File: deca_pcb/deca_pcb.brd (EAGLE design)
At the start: 68.2 x 80 mm, 3 parts, among them IC1 DWM1000, U1 ATMEGA328P-PU

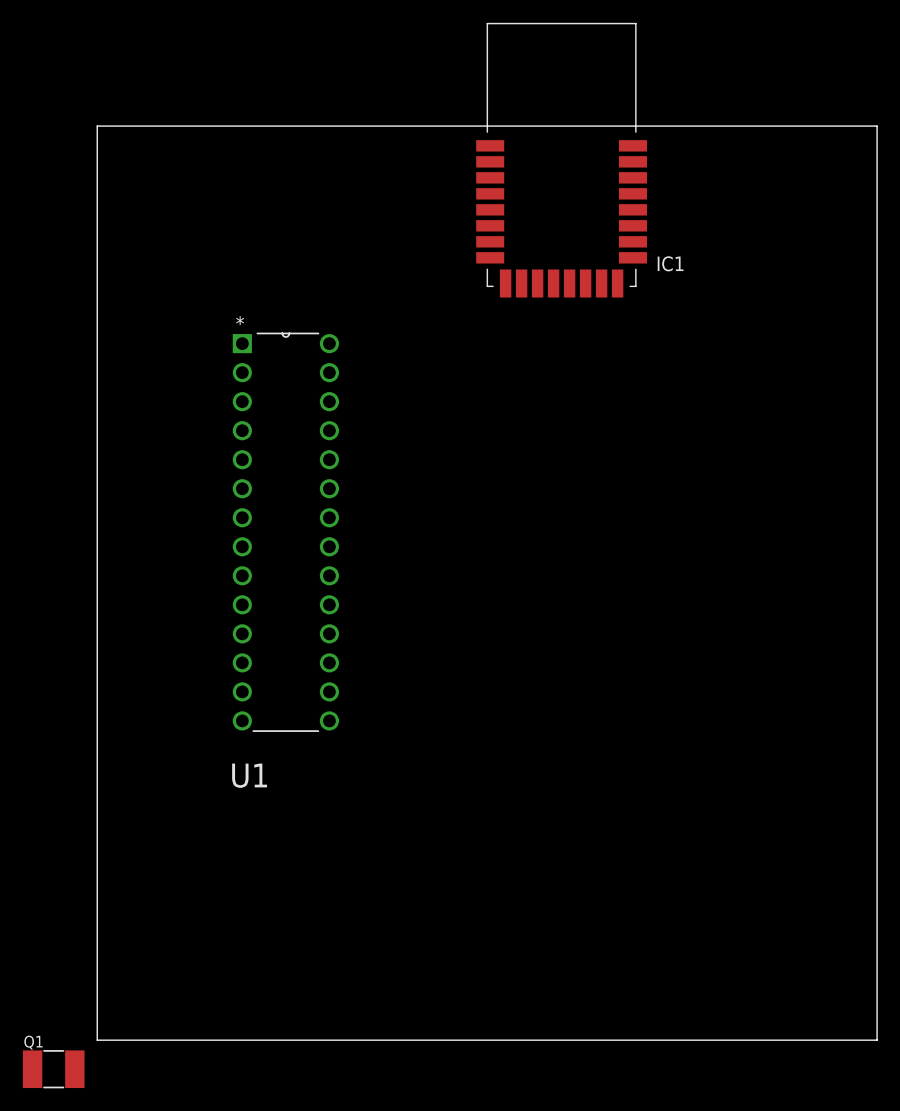
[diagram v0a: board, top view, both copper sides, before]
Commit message: added components
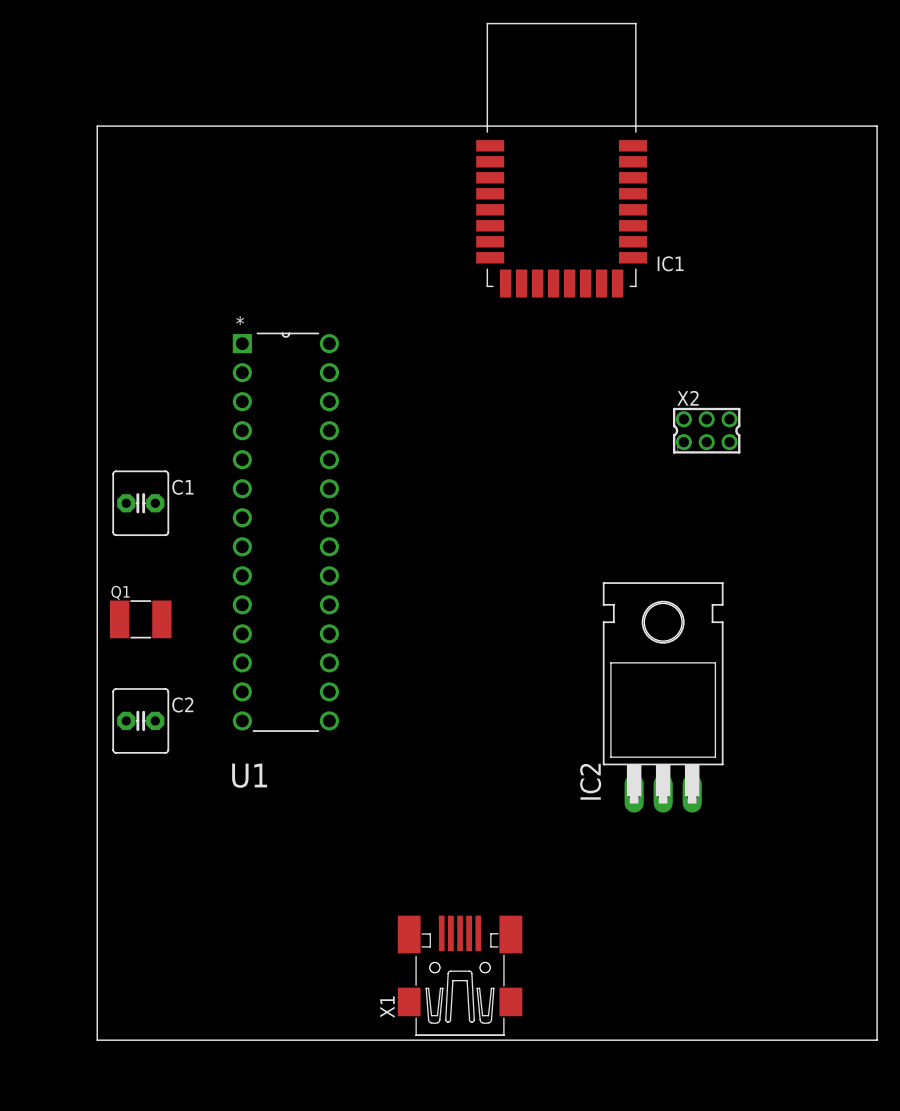
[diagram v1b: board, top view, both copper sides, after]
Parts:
- added C1, C2: (no value), capacitor-wima:C2.5-6
- added IC2: LM340H-18, linear:TO220H
- added X1: MINI-USB-32005-301, con-cypressindustries:32005-301
- added X2: 332-06, con-garry:332-06
- moved Q1 40.1 mm to (3.81, 36.8)
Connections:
- removed net AVCC: U1.20
- removed net VCC: U1.7
- new net N$10: IC2.1, X1.1
- new net N$11: C1.2, C2.1, IC1.16, IC1.21, IC1.23, IC1.24, IC1.8, IC2.2, U1.22, U1.8, X1.5, X2.6
- new net N$12: IC1.5, IC1.6, IC1.7, IC2.3, U1.20, U1.7, X2.2
- new net N$9: U1.1, X2.5
- net N$1: now also X2.3
- net N$2: now also X2.1
- net N$3: now also X2.4
- net N$7: now also C2.2
- net N$8: now also C1.1
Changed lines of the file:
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@@
 <attribute name="VALUE" x="13.0556" y="64.135" size="2.0828" layer="27" ratio="10" rot="SR0"/>
 </element>
-<element name="Q1" library="crystal-geyer_V1_0" library_urn="urn:adsk.eagle:library:203" package="5.0X3.2_2" package3d_urn="urn:adsk.eagle:package:11930/1" value="" x="-3.81" y="-2.54" smashed="yes">
-<attribute name="NAME" x="-6.45" y="-0.64" size="1.016" layer="25"/>
-<attribute name="VALUE" x="-6.45" y="-5.44" size="1.016" layer="27"/>
+<element name="Q1" library="crystal-geyer_V1_0" library_urn="urn:adsk.eagle:library:203" package="5.0X3.2_2" package3d_urn="urn:adsk.eagle:package:11930/1" value="" x="3.81" y="36.83" smashed="yes">
+<attribute name="NAME" x="1.17" y="38.73" size="1.016" layer="25"/>
+<attribute name="VALUE" x="1.17" y="33.93" size="1.016" layer="27"/>
+</element>
+<element name="C1" library="capacitor-wima" library_urn="urn:adsk.eagle:library:116" package="C2.5-6" package3d_urn="urn:adsk.eagle:package:5406/1" value="" x="3.81" y="46.99" smashed="yes">
+<attribute name="NAME" x="6.477" y="47.752" size="1.27" layer="25" ratio="10"/>
+<attribute name="VALUE" x="1.905" y="44.577" size="1.27" layer="27" ratio="10"/>
+</element>
+<element name="C2" library="capacitor-wima" library_urn="urn:adsk.eagle:library:116" package="C2.5-6" package3d_urn="urn:adsk.eagle:package:5406/1" value="" x="3.81" y="27.94" smashed="yes">
+<attribute name="NAME" x="6.477" y="28.702" size="1.27" layer="25" ratio="10"/>
+<attribute name="VALUE" x="1.905" y="25.527" size="1.27" layer="27" ratio="10"/>
+</element>
+<element name="X1" library="con-cypressindustries" library_urn="urn:adsk.eagle:library:138" package="32005-301" package3d_urn="urn:adsk.eagle:package:6446/1" value="MINI-USB-32005-301" x="31.75" y="6.35" smashed="yes" rot="R90">
+<attribute name="MF" value="" x="31.75" y="6.35" size="1.778" layer="27" rot="R90" display="off"/>
+<attribute name="MPN" value="" x="31.75" y="6.35" size="1.778" layer="27" rot="R90" display="off"/>
+<attribute name="NAME" x="26.035" y="1.905" size="1.27" layer="25" rot="R90"/>
+<attribute name="OC_FARNELL" value="unknown" x="31.75" y="6.35" size="1.778" layer="27" rot="R90" display="off"/>
+<attribute name="OC_NEWARK" value="unknown" x="31.75" y="6.35" size="1.778" layer="27" rot="R90" display="off"/>
+<attribute name="VALUE" x="38.735" y="1.905" size="1.27" layer="27" rot="R90"/>
+</element>
+<element name="IC2" library="linear" library_urn="urn:adsk.eagle:library:262" package="TO220H" package3d_urn="urn:adsk.eagle:package:16414/1" value="LM340H-18" x="49.53" y="31.75" smashed="yes">
+<attribute name="NAME" x="44.069" y="20.828" size="1.778" layer="25" ratio="10" rot="R90"/>
+<attribute name="VALUE" x="56.896" y="20.701" size="1.778" layer="27" ratio="10" rot="R90"/>
+</element>
+<element name="X2" library="con-garry" library_urn="urn:adsk.eagle:library:147" package="332-06" package3d_urn="urn:adsk.eagle:package:6811/1" value="332-06" x="53.34" y="53.34" smashed="yes">
+<attribute name="NAME" x="50.72" y="55.53" size="1.27" layer="25"/>
+<attribute name="VALUE" x="50.72" y="56.88" size="1.27" layer="27"/>
 </element>
 </elements>
 <signals>
-<signal name="VCC">
-<contactref element="U1" pad="7"/>
-</signal>
-<signal name="AVCC">
-<contactref element="U1" pad="20"/>
-</signal>
 <signal name="N$1">
 <contactref element="U1" pad="19"/>
 <contactref element="IC1" pad="20"/>
+<contactref element="X2" pad="3"/>
 <wire x1="20.32" y1="38.1" x2="46.89" y2="72.67" width="0" layer="19" extent="1-1"/>
+<wire x1="53.34" y1="52.34" x2="20.32" y2="38.1" width="0" layer="19" extent="1-1"/>
 </signal>
 <signal name="N$2">
 <contactref element="U1" pad="18"/>
 <contactref element="IC1" pad="19"/>
+<contactref element="X2" pad="1"/>
 <wire x1="20.32" y1="35.56" x2="46.89" y2="71.27" width="0" layer="19" extent="1-1"/>
+<wire x1="51.34" y1="52.34" x2="20.32" y2="35.56" width="0" layer="19" extent="1-1"/>
 </signal>
 <signal name="N$3">
 <contactref element="U1" pad="17"/>
 <contactref element="IC1" pad="18"/>
+<contactref element="X2" pad="4"/>
 <wire x1="20.32" y1="33.02" x2="46.89" y2="69.87" width="0" layer="19" extent="1-1"/>
+<wire x1="53.34" y1="54.34" x2="20.32" y2="33.02" width="0" layer="19" extent="1-1"/>
 </signal>
 <signal name="N$4">
@@
 <contactref element="U1" pad="9"/>
 <contactref element="Q1" pad="2"/>
-<wire x1="-1.96" y1="-2.54" x2="12.7" y2="40.64" width="0" layer="19" extent="1-1"/>
+<contactref element="C2" pad="2"/>
+<wire x1="5.66" y1="36.83" x2="12.7" y2="40.64" width="0" layer="19" extent="1-1"/>
+<wire x1="5.08" y1="27.94" x2="5.66" y2="36.83" width="0" layer="19" extent="1-1"/>
 </signal>
 <signal name="N$8">
 <contactref element="U1" pad="10"/>
 <contactref element="Q1" pad="1"/>
-<wire x1="-5.66" y1="-2.54" x2="12.7" y2="38.1" width="0" layer="19" extent="1-1"/>
+<contactref element="C1" pad="1"/>
+<wire x1="1.96" y1="36.83" x2="12.7" y2="38.1" width="0" layer="19" extent="1-1"/>
+<wire x1="2.54" y1="46.99" x2="1.96" y2="36.83" width="0" layer="19" extent="1-1"/>
+</signal>
+<signal name="N$10">
+<contactref element="X1" pad="1"/>
+<contactref element="IC2" pad="1"/>
+<wire x1="30.15" y1="9.35" x2="46.99" y2="21.59" width="0" layer="19" extent="1-1"/>
+</signal>
+<signal name="N$11">
+<contactref element="X1" pad="5"/>
+<contactref element="IC2" pad="2"/>
+<contactref element="C1" pad="2"/>
+<contactref element="C2" pad="1"/>
+<contactref element="U1" pad="22"/>
+<contactref element="U1" pad="8"/>
+<contactref element="IC1" pad="21"/>
+<contactref element="IC1" pad="16"/>
+<contactref element="IC1" pad="23"/>
+<contactref element="IC1" pad="24"/>
+<contactref element="IC1" pad="8"/>
+<contactref element="X2" pad="6"/>
+<wire x1="46.89" y1="78.27" x2="46.89" y2="76.87" width="0" layer="19" extent="1-1"/>
+<wire x1="46.89" y1="74.07" x2="46.89" y2="76.87" width="0" layer="19" extent="1-1"/>
+<wire x1="45.54" y1="66.22" x2="46.89" y2="74.07" width="0" layer="19" extent="1-1"/>
+<wire x1="34.39" y1="68.47" x2="45.54" y2="66.22" width="0" layer="19" extent="1-1"/>
+<wire x1="20.32" y1="45.72" x2="34.39" y2="68.47" width="0" layer="19" extent="1-1"/>
+<wire x1="12.7" y1="43.18" x2="20.32" y2="45.72" width="0" layer="19" extent="1-1"/>
+<wire x1="5.08" y1="46.99" x2="12.7" y2="43.18" width="0" layer="19" extent="1-1"/>
+<wire x1="2.54" y1="27.94" x2="12.7" y2="43.18" width="0" layer="19" extent="1-1"/>
+<wire x1="55.34" y1="54.34" x2="2.54" y2="27.94" width="0" layer="19" extent="1-1"/>
+<wire x1="33.35" y1="9.35" x2="2.54" y2="27.94" width="0" layer="19" extent="1-1"/>
+<wire x1="49.53" y1="21.59" x2="33.35" y2="9.35" width="0" layer="19" extent="1-1"/>
+</signal>
+<signal name="N$12">
+<contactref element="IC2" pad="3"/>
+<contactref element="U1" pad="7"/>
+<contactref element="U1" pad="20"/>
+<contactref element="IC1" pad="5"/>
+<contactref element="IC1" pad="6"/>
+<contactref element="IC1" pad="7"/>
+<contactref element="X2" pad="2"/>
+<wire x1="34.39" y1="71.27" x2="34.39" y2="72.67" width="0" layer="19" extent="1-1"/>
+<wire x1="34.39" y1="69.87" x2="34.39" y2="71.27" width="0" layer="19" extent="1-1"/>
+<wire x1="20.32" y1="40.64" x2="34.39" y2="69.87" width="0" layer="19" extent="1-1"/>
+<wire x1="12.7" y1="45.72" x2="20.32" y2="40.64" width="0" layer="19" extent="1-1"/>
+<wire x1="52.07" y1="21.59" x2="20.32" y2="40.64" width="0" layer="19" extent="1-1"/>
+<wire x1="51.34" y1="54.34" x2="20.32" y2="40.64" width="0" layer="19" extent="1-1"/>
+</signal>
+<signal name="N$9">
+<contactref element="U1" pad="1"/>
+<contactref element="X2" pad="5"/>
+<wire x1="55.34" y1="52.34" x2="12.7" y2="60.96" width="0" layer="19" extent="1-1"/>
 </signal>
 </signals>

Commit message: board pcb done
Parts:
- removed IC2: LM340H-18, linear:TO220H
- removed Q1: (no value), crystal-geyer_V1_0:5.0X3.2_2
- removed X2: 332-06, con-garry:332-06
- added C3: (no value), microbuilder:CELEC_3.5MM_8MM
- added IC3: (no value), lf33:TO220S
- added JP1, JP2, JP3, JP4, JP7: (no value), jumper:JP1
- added JP10, JP12, JP13, JP14, JP15, JP5, JP6, JP8, JP9: (no value), con-pinhead:1X01
- added TR1: (no value), discrete:R-5
- moved IC1 40.1 mm to (48.3, 38.1), turned to 270 degrees
- moved U1 26.7 mm to (31.8, 3.81)
- moved X1 24.1 mm to (7.62, 6.35)
- moved C1 5.08 mm to (3.81, 41.9), turned to 90 degrees
- turned C2 to 90 degrees
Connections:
- new net N$13: C1.2, C2.1, IC1.16, IC1.21, IC1.23, IC1.24, IC1.8, IC3.2, JP6.1, TR1.2, U1.22, U1.8, X1.5
- new net N$14: IC1.19, JP2.1
- new net N$15: IC1.18, JP3.1
- new net N$16: IC1.17, JP4.1
- new net N$17: JP8.1, U1.2
- new net N$18: JP9.1, U1.3
- new net N$19: JP12.1, U1.1
- net N$1: now also JP1.2, JP15.1; no longer IC1.20, X2.3
- net N$10: now also IC3.1, JP5.1; no longer IC2.1
- net N$11: now also IC1.20, JP1.1; no longer C1.2, C2.1, IC1.16, IC1.21, IC1.23, IC1.24, IC1.8, IC2.2, U1.22, U1.8, X1.5, X2.6
- net N$12: now also IC3.3, JP10.1, JP7.1; no longer IC1.5, IC1.6, IC1.7, IC2.3, X2.2
- net N$2: now also JP14.1, JP2.2; no longer IC1.19, X2.1
- net N$3: now also JP13.1, JP3.2; no longer IC1.18, X2.4
- net N$4: now also JP4.2; no longer IC1.17
- net N$5: now also TR1.1
- net N$7: now also C3.+; no longer Q1.2
- net N$8: now also C3.-; no longer Q1.1
- net N$9: now also IC1.5, IC1.6, IC1.7, JP7.2; no longer U1.1, X2.5
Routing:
- net N$13: track 0.00 -> 161.9 mm
- net N$5: track 0.00 -> 83.6 mm
- net N$12: track 0.00 -> 65.9 mm
- net N$6: track 0.00 -> 63.2 mm
- net N$8: track 0.00 -> 48.5 mm
- net N$1: track 0.00 -> 47.5 mm
- net N$7: track 0.00 -> 38.9 mm
- net N$2: track 0.00 -> 31.0 mm
- net N$3: track 0.00 -> 26.4 mm
- net N$9: track 0.00 -> 18.2 mm
- net N$4: track 0.00 -> 16.8 mm
- net N$10: track 0.00 -> 14.0 mm
- net N$11: track 0.00 -> 12.2 mm
- net N$16: track 0.00 -> 11.3 mm
- net N$14: track 0.00 -> 11.3 mm
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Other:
- board size 68.2 x 80 mm -> 51.7 x 49.5 mm

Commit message: txt
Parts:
- removed C3: (no value), microbuilder:CELEC_3.5MM_8MM
- added Q1: (no value), crystal:HC49/S
- moved C1 38.7 mm to (19.1, 6.35), turned to 270 degrees
- moved C2 15.7 mm to (19.1, 24.1)
- moved JP10 12.7 mm to (11.4, 24.1)
- moved JP9 3.81 mm to (16.5, 31.8)
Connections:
- net N$12 renamed VCC
- net N$17 renamed JP8
- removed net N$13: C1.2, C2.1, IC1.16, IC1.21, IC1.23, IC1.24, IC1.8, IC3.2, JP6.1, TR1.2, U1.22, U1.8, X1.5
- new net GND: C1.2, C2.2, IC1.16, IC1.21, IC1.23, IC1.24, IC1.8, IC3.2, JP6.1, TR1.2, U1.22, U1.8, X1.5
- net N$7: now also C2.1, Q1.1; no longer C2.2, C3.+
- net N$8: now also Q1.2; no longer C3.-
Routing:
- net N$13: track 161.9 -> 0.00 mm
- net GND: track 0.00 -> 125.5 mm
- net VCC: track 65.9 -> 0.00 mm
- net N$8: track 48.5 -> 10.8 mm
- net N$7: track 38.9 -> 10.8 mm
- net JP8: track 7.62 -> 0.00 mm
- net N$18: track 9.20 -> 7.62 mm
- added copper zone on layer 1, net GND
